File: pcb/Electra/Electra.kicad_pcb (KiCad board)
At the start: 2 copper layers, 100 x 48.5 mm, 79 parts, among them J101 RTC, J102 UART, J201 8-28VIn, J202 USB_B_Micro, J203 Enable VIn, J301 Relay2/D, J401 Relay1/U, J501 S1/U, J502 S2/D, J701 A, J702 A2, J801 RF433, K301 FINDER-36.11, K401 FINDER-36.11, Q301 Q_NPN_EBC, Q401 Q_NPN_EBC, Q801 BSS138, SW601 Flash, SW602 RST, U201 AMS1117-3.3, U202 TPS54202DDCR, U601 ESP-12F

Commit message: PCB Ver 1 completed (TODO: Check)
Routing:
- net +3V3: track 191.2 -> 189.4 mm
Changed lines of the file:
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@@
       (effects (font (size 1 1) (thickness 0.15)))
     )
-    (fp_text value RF433 (at -0.8 -2.4 90) (layer F.SilkS)
+    (fp_text value RF433 (at 0 -4.2 180) (layer F.SilkS)
       (effects (font (size 1 1) (thickness 0.15)))
     )
@@
     (effects (font (size 0.9 0.9) (thickness 0.15)))
   )
-  (gr_text SDL (at 117.4 105.7) (layer F.SilkS)
+  (gr_text SDL (at 122.75 105.7) (layer F.SilkS)
     (effects (font (size 0.9 0.9) (thickness 0.15)))
   )
-  (gr_text SDA (at 117.3 103.2) (layer F.SilkS)
+  (gr_text SDA (at 122.65 102.9) (layer F.SilkS)
     (effects (font (size 0.9 0.9) (thickness 0.15)))
   )
-  (gr_text 3V3 (at 117.4 100.6) (layer F.SilkS)
+  (gr_text 3V3 (at 122.55 100.7) (layer F.SilkS)
     (effects (font (size 0.9 0.9) (thickness 0.15)))
   )
-  (gr_text GND (at 117.3 98) (layer F.SilkS)
+  (gr_text GND (at 119.95 95.85) (layer F.SilkS)
     (effects (font (size 0.9 0.9) (thickness 0.15)))
   )
@@
   (via (at 115.25 116) (size 0.8) (drill 0.4) (layers F.Cu B.Cu) (net 2))
   (via (at 116.25 116) (size 0.8) (drill 0.4) (layers F.Cu B.Cu) (net 2))
-  (via (at 122 106.5) (size 0.8) (drill 0.4) (layers F.Cu B.Cu) (net 2))
-  (via (at 123.25 106.5) (size 0.8) (drill 0.4) (layers F.Cu B.Cu) (net 2))
+  (via (at 122 106.65) (size 0.8) (drill 0.4) (layers F.Cu B.Cu) (net 2))
+  (via (at 123.25 106.7) (size 0.8) (drill 0.4) (layers F.Cu B.Cu) (net 2))
   (via (at 122 107.75) (size 0.8) (drill 0.4) (layers F.Cu B.Cu) (net 2))
   (via (at 123.25 107.75) (size 0.8) (drill 0.4) (layers F.Cu B.Cu) (net 2))
@@
   (segment (start 160 113.12) (end 157.12 113.12) (width 0.5) (layer F.Cu) (net 3))
   (segment (start 157.12 113.12) (end 153.25 109.25) (width 0.5) (layer F.Cu) (net 3))
-  (segment (start 126.6125 92.4745) (end 125.324 91.186) (width 0.7) (layer F.Cu) (net 3))
   (segment (start 128.334 94.25) (end 128.25 94.25) (width 0.7) (layer B.Cu) (net 3))
   (segment (start 126.964 92.964) (end 128.25 94.25) (width 0.7) (layer B.Cu) (net 3))
@@
   (segment (start 153.25 97.75) (end 155.85 95.15) (width 0.5) (layer F.Cu) (net 3))
   (segment (start 155.85 90.091998) (end 155.85 95.15) (width 0.5) (layer F.Cu) (net 3))
-  (segment (start 126.0625 91.9245) (end 125.324 91.186) (width 0.7) (layer F.Cu) (net 3))
-  (segment (start 126.0625 96.1) (end 126.0625 91.9245) (width 0.7) (layer F.Cu) (net 3))
   (segment (start 126.0625 97.8) (end 126.0625 96.1) (width 0.7) (layer F.Cu) (net 3))
   (segment (start 126.4 96.1) (end 128.25 94.25) (width 0.7) (layer F.Cu) (net 3))
   (segment (start 126.0625 96.1) (end 126.4 96.1) (width 0.7) (layer F.Cu) (net 3))
+  (segment (start 125.95 91.812) (end 125.324 91.186) (width 0.7) (layer F.Cu) (net 3))
+  (segment (start 126.0625 96.1) (end 125.95 95.9875) (width 0.7) (layer F.Cu) (net 3))
+  (segment (start 125.95 95.9875) (end 125.95 91.812) (width 0.7) (layer F.Cu) (net 3))
   (via (at 104.8 101.9) (size 0.8) (drill 0.4) (layers F.Cu B.Cu) (net 4))
   (via (at 104.8 104.2) (size 0.8) (drill 0.4) (layers F.Cu B.Cu) (net 4))

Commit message: PCB completed (added silkscreen more)
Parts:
- added G***: LOGO, Custom:Electricity-Causion-6.1mmX6.1mm-logo, B.Cu at (177.0, 100.6)
- added G***: LOGO, Custom:Recycle-electronics-10mmx10mm-logo, B.Cu at (111.5, 99.5)
- added G***: LOGO, Custom:Recycle-electronics-10mmx10mm-logo, F.Cu at (148.0, 98.7)
- added G***: LOGO, Custom:Electricity-Causion-3mmX3mm, F.Cu at (195.0, 102.7)
- J201: value 8-28VIn -> 8-28V
- J202: value USB_B_Micro -> USB
- J301: value Relay2/D -> Relay 2/D
- J401: value Relay1/U -> Relay 1/U
- moved TP301 1.53 mm to (178.3, 109.1)
- moved TP401 1.41 mm to (178.2, 106.5)
- moved C601 0.91 mm to (126.1, 96.0)
- moved C602 0.91 mm to (126.1, 97.7)
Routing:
- net /ESP8266/ADC: track 54.8 -> 56.4 mm
- net +3V3: track 189.4 -> 190.9 mm
- net /Relay1: track 72.9 -> 74.3 mm
- net +5V: track 178.5 -> 179.4 mm
- net /TX: track 43.6 -> 44.5 mm
- net Net-(J601-Pad4): vias 1 -> 0
- net GND: vias 557 -> 556
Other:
- outline, holes or cut-outs redrawn
- board text added: "+"
- board text added: "-"
- board text added: "0603-1210"
- board text added: "10K"
- board text added: "10x10"
- board text added: "CAUTION! AC Voltage"
- board text added: "If you are reading this, I hope you have a nice day!"
- board text added: "NC"
- board text added: "NO"
- board text added: "R20X"
- board text removed: "CAUTION! AC Main"

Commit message: Pcb completed with 3D model
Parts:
- removed the G*** at (111.5, 99.5)
- removed the G*** at (148.0, 98.7)
- moved J201 2.22 mm to (108.0, 81.0)
- moved J801 1.40 mm to (146.6, 86.7)
- moved C208 0.69 mm to (123.2, 83.3)
- moved C203 0.56 mm to (116.8, 83.3)
- moved J501 0.44 mm to (154.5, 76.3)
- moved J701 0.44 mm to (136.7, 76.3)
- moved J702 0.44 mm to (128.1, 76.3)
- moved J502 0.44 mm to (145.6, 76.3)
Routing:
- net /Switch1: track 66.1 -> 49.5 mm, vias 0 -> 1
- net +3V3: track 190.9 -> 196.3 mm
- net /Switch2: track 43.9 -> 39.3 mm, vias 0 -> 1
- net +5V: track 179.4 -> 176.2 mm
- net Net-(J702-Pad1): track 8.60 -> 10.9 mm, vias 0 -> 2
- net /ESP8266/ADC: track 56.4 -> 55.3 mm
- net /ESP8266/GPIO0: track 49.2 -> 48.6 mm
- net GND: vias 556 -> 569
- net +VDC: vias 11 -> 18

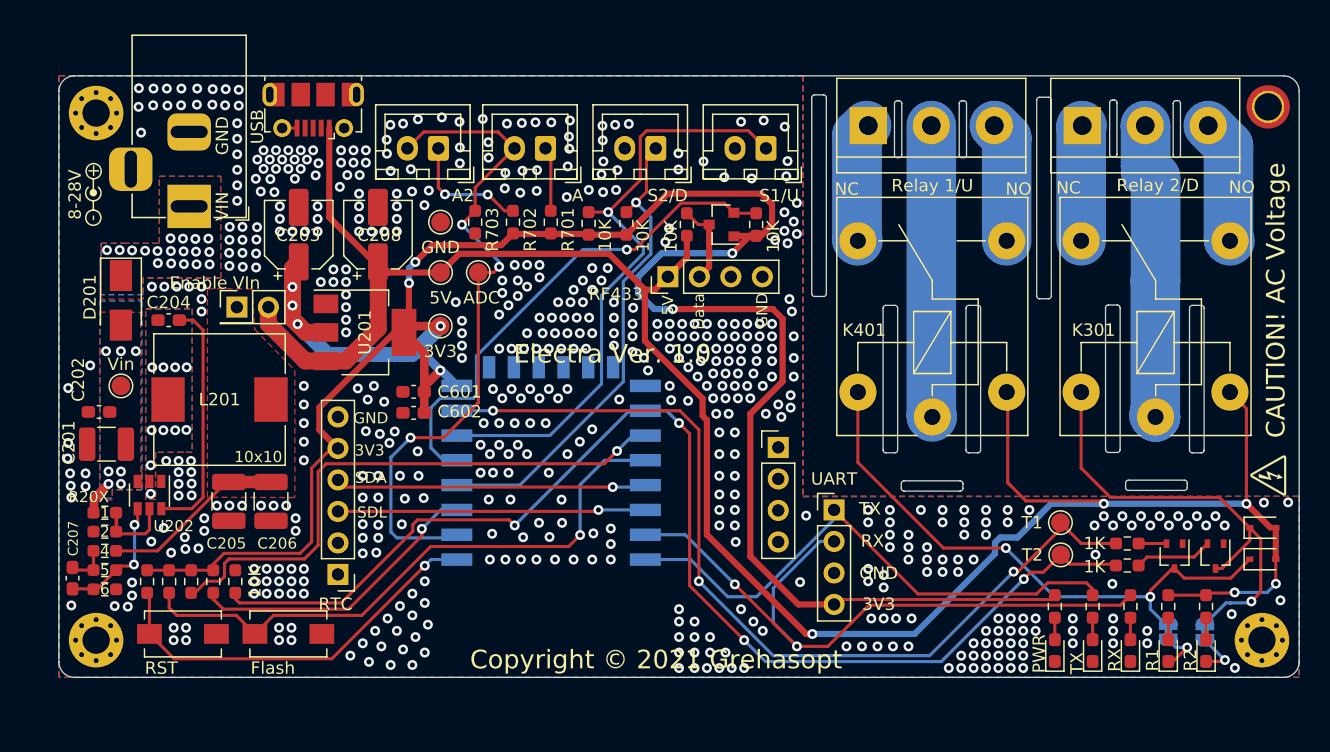
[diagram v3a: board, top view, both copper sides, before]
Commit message: Panel added, gerbs added
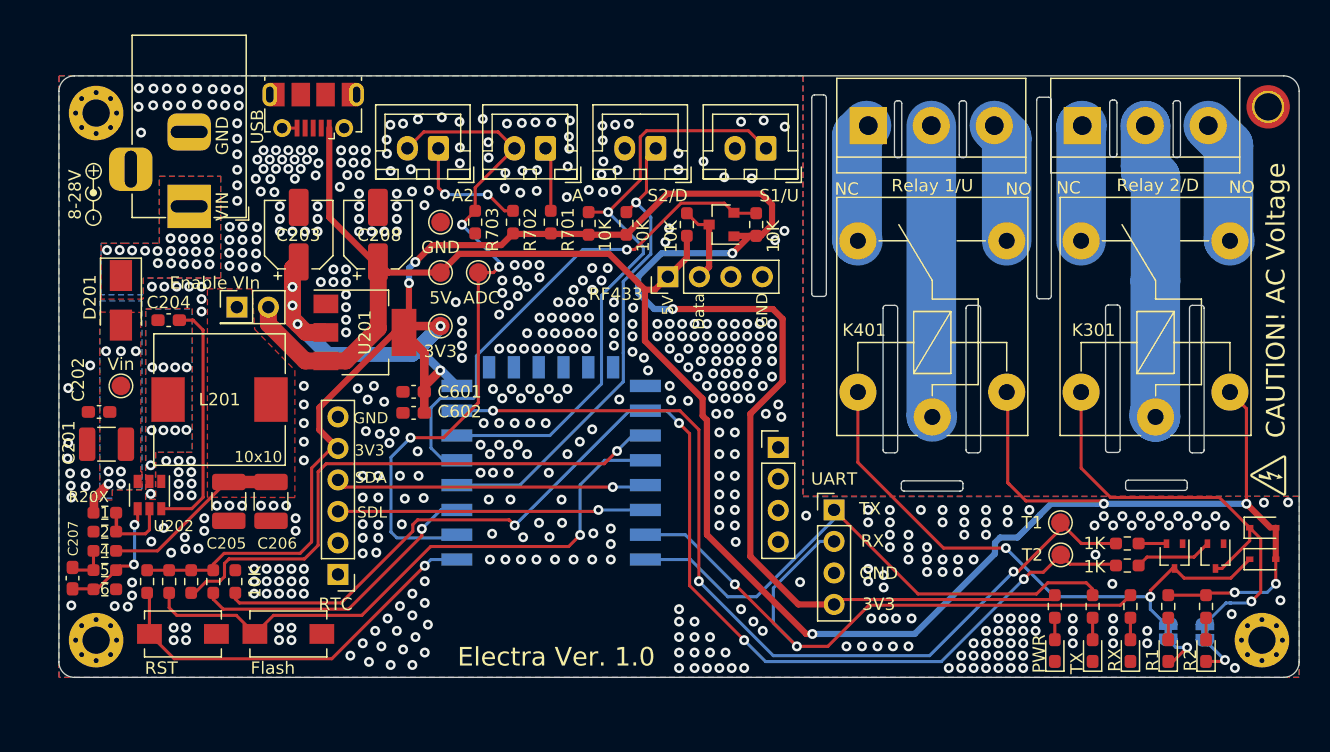
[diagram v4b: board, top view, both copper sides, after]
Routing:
- net GND: vias 569 -> 555
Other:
- board text removed: "Copyright © 2021 Grehasopt"
- board text removed: "JLCJLCJLCJLC"
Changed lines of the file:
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@@
   (general
     (thickness 1.6)
-    (drawings 145)
-    (tracks 1093)
+    (drawings 143)
+    (tracks 1079)
     (zones 0)
     (modules 81)
@@
     (pad_to_mask_clearance 0)
     (aux_axis_origin 0 0)
+    (grid_origin 97.5 70.5)
     (visible_elements FFFFEF7F)
     (pcbplotparams
       (layerselection 0x010f0_ffffffff)
       (usegerberextensions false)
-      (usegerberattributes true)
-      (usegerberadvancedattributes true)
-      (creategerberjobfile true)
+      (usegerberattributes false)
+      (usegerberadvancedattributes false)
+      (creategerberjobfile false)
       (excludeedgelayer true)
       (linewidth 0.100000)
@@
       (drillshape 0)
       (scaleselection 1)
-      (outputdirectory "gerbers/"))
+      (outputdirectory "gerber/single/"))
   )
   (net 0 "")
@@
       (effects (font (size 0.8 0.8) (thickness 0.12)))
     )
-    (pad 2 smd roundrect (at 1.5625 0 180) (size 1.325 2.7) (layers F.Cu F.Paste F.Mask) (roundrect_rratio 0.1886784905660377)
+    (pad 2 smd roundrect (at 1.5625 0 180) (size 1.325 2.7) (layers F.Cu F.Paste F.Mask) (roundrect_rratio 0.1886769811320755)
       (net 2 GND))
-    (pad 1 smd roundrect (at -1.5625 0 180) (size 1.325 2.7) (layers F.Cu F.Paste F.Mask) (roundrect_rratio 0.1886784905660377)
+    (pad 1 smd roundrect (at -1.5625 0 180) (size 1.325 2.7) (layers F.Cu F.Paste F.Mask) (roundrect_rratio 0.1886769811320755)
       (net 1 "Net-(C201-Pad1)"))
     (model ${KISYS3DMOD}/Capacitor_SMD.3dshapes/C_1210_3225Metric.wrl
@@
       (effects (font (size 0.8 0.8) (thickness 0.12)))
     )
-    (pad 1 smd roundrect (at -1.5625 0 90) (size 1.325 2.7) (layers F.Cu F.Paste F.Mask) (roundrect_rratio 0.1886784905660377)
+    (pad 1 smd roundrect (at -1.5625 0 90) (size 1.325 2.7) (layers F.Cu F.Paste F.Mask) (roundrect_rratio 0.1886769811320755)
       (net 2 GND))
-    (pad 2 smd roundrect (at 1.5625 0 90) (size 1.325 2.7) (layers F.Cu F.Paste F.Mask) (roundrect_rratio 0.1886784905660377)
+    (pad 2 smd roundrect (at 1.5625 0 90) (size 1.325 2.7) (layers F.Cu F.Paste F.Mask) (roundrect_rratio 0.1886769811320755)
       (net 6 "Net-(C205-Pad2)"))
     (model ${KISYS3DMOD}/Capacitor_SMD.3dshapes/C_1210_3225Metric.wrl
@@
       (effects (font (size 0.8 0.8) (thickness 0.12)))
     )
-    (pad 2 smd roundrect (at 1.5625 0 90) (size 1.325 2.7) (layers F.Cu F.Paste F.Mask) (roundrect_rratio 0.1886784905660377)
+    (pad 2 smd roundrect (at 1.5625 0 90) (size 1.325 2.7) (layers F.Cu F.Paste F.Mask) (roundrect_rratio 0.1886769811320755)
       (net 6 "Net-(C205-Pad2)"))
-    (pad 1 smd roundrect (at -1.5625 0 90) (size 1.325 2.7) (layers F.Cu F.Paste F.Mask) (roundrect_rratio 0.1886784905660377)
+    (pad 1 smd roundrect (at -1.5625 0 90) (size 1.325 2.7) (layers F.Cu F.Paste F.Mask) (roundrect_rratio 0.1886769811320755)
       (net 2 GND))
     (model ${KISYS3DMOD}/Capacitor_SMD.3dshapes/C_1210_3225Metric.wrl
@@
     (effects (font (size 1 1) (thickness 0.25)))
   )
-  (gr_text JLCJLCJLCJLC (at 196.3 90.25 90) (layer B.SilkS)
-    (effects (font (size 1 1) (thickness 0.25)) (justify mirror))
-  )
   (gr_text "CAUTION! AC Voltage" (at 195.625 88.6 90) (layer F.SilkS)
     (effects (font (size 1.5 1.5) (thickness 0.3)))
@@
     (effects (font (size 1 1) (thickness 0.15)))
   )
-  (gr_text "Copyright © 2021 Grehasopt " (at 145.65 117.575) (layer F.SilkS)
-    (effects (font (size 1.5 1.5) (thickness 0.3)))
-  )
-  (gr_text "Electra Ver. 1.0" (at 142.125 92.925) (layer F.SilkS)
+  (gr_text "Electra Ver. 1.0" (at 137.6 117.35) (layer F.SilkS)
     (effects (font (size 1.5 1.5) (thickness 0.3)))
   )
@@
   (via (at 154.5 97.75) (size 0.8) (drill 0.4) (layers F.Cu B.Cu) (net 2))
   (via (at 155.5 97) (size 0.8) (drill 0.4) (layers F.Cu B.Cu) (net 2))
-  (via (at 156.5 96.25) (size 0.8) (drill 0.4) (layers F.Cu B.Cu) (net 2))
   (via (at 155.75 98) (size 0.8) (drill 0.4) (layers F.Cu B.Cu) (net 2))
-  (via (at 156.5 97.25) (size 0.8) (drill 0.4) (layers F.Cu B.Cu) (net 2))
   (via (at 155.25 83.75) (size 0.8) (drill 0.4) (layers F.Cu B.Cu) (net 2))
-  (via (at 156 83) (size 0.8) (drill 0.4) (layers F.Cu B.Cu) (net 2))
-  (via (at 156.75 82.25) (size 0.8) (drill 0.4) (layers F.Cu B.Cu) (net 2))
-  (via (at 156.25 84) (size 0.8) (drill 0.4) (layers F.Cu B.Cu) (net 2))
-  (via (at 157 83.25) (size 0.8) (drill 0.4) (layers F.Cu B.Cu) (net 2))
-  (via (at 156 81.5) (size 0.8) (drill 0.4) (layers F.Cu B.Cu) (net 2))
-  (via (at 157 80.75) (size 0.8) (drill 0.4) (layers F.Cu B.Cu) (net 2))
-  (via (at 156.75 94.75) (size 0.8) (drill 0.4) (layers F.Cu B.Cu) (net 2))
-  (via (at 156.75 93.25) (size 0.8) (drill 0.4) (layers F.Cu B.Cu) (net 2))
-  (via (at 156.75 91.5) (size 0.8) (drill 0.4) (layers F.Cu B.Cu) (net 2))
   (via (at 112 71.625) (size 0.8) (drill 0.4) (layers F.Cu B.Cu) (net 2))
   (via (at 110.95 71.575) (size 0.8) (drill 0.4) (layers F.Cu B.Cu) (net 2))
@@
   (via (at 111.875 80.575) (size 0.8) (drill 0.4) (layers F.Cu B.Cu) (net 2))
   (via (at 104.125 75.075) (size 0.8) (drill 0.4) (layers F.Cu B.Cu) (net 2))
-  (via (at 156.4 88.5) (size 0.8) (drill 0.4) (layers F.Cu B.Cu) (net 2))
-  (via (at 156.6 89.5) (size 0.8) (drill 0.4) (layers F.Cu B.Cu) (net 2))
   (via (at 143.8 89.2) (size 0.8) (drill 0.4) (layers F.Cu B.Cu) (net 2))
   (via (at 146.4 83.9) (size 0.8) (drill 0.4) (layers F.Cu B.Cu) (net 2))
@@
   (via (at 151.15 78.675) (size 0.8) (drill 0.4) (layers F.Cu B.Cu) (net 2))
   (via (at 153.35 78.775) (size 0.8) (drill 0.4) (layers F.Cu B.Cu) (net 2))
-  (via (at 156.15 78.6) (size 0.8) (drill 0.4) (layers F.Cu B.Cu) (net 2))
-  (via (at 156.25 77.375) (size 0.8) (drill 0.4) (layers F.Cu B.Cu) (net 2))
-  (via (at 156.025 74.6) (size 0.8) (drill 0.4) (layers F.Cu B.Cu) (net 2))
   (via (at 154.325 74.1) (size 0.8) (drill 0.4) (layers F.Cu B.Cu) (net 2))
   (via (at 152.5 74.2) (size 0.8) (drill 0.4) (layers F.Cu B.Cu) (net 2))
@@
   (via (at 112.3 82.675) (size 0.8) (drill 0.4) (layers F.Cu B.Cu) (net 2))
   (via (at 113.475 82.7) (size 0.8) (drill 0.4) (layers F.Cu B.Cu) (net 2))
+  (via (at 156.025 74.6) (size 0.8) (drill 0.4) (layers F.Cu B.Cu) (net 2))
+  (via (at 156 83) (size 0.8) (drill 0.4) (layers F.Cu B.Cu) (net 2))
   (segment (start 117.413998 91.186) (end 119.024 91.186) (width 1.37) (layer F.Cu) (net 3))
   (via (at 125.73 87.21) (size 0.8) (drill 0.4) (layers F.Cu B.Cu) (net 3))

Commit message: Rev 2 completed, todo check all and remove not needed filed
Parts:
- removed C206: 22uF, Capacitor_SMD:C_1210_3225Metric_Pad1.33x2.70mm_HandSolder
- removed C207: 75pF, Capacitor_SMD:C_0603_1608Metric_Pad1.08x0.95mm_HandSolder
- removed C208: 100uF, Capacitor_SMD:CP_Elec_5x5.4
- removed C601: 0.1uF, Capacitor_SMD:C_0603_1608Metric_Pad1.08x0.95mm_HandSolder
- removed C602: 47uF, Capacitor_SMD:C_0603_1608Metric_Pad1.08x0.95mm_HandSolder
- removed D401: R1, LED_SMD:LED_0603_1608Metric_Pad1.05x0.95mm_HandSolder
- removed D402: 200mA, Diode_SMD:D_SOD-323
- removed D601: TX, LED_SMD:LED_0603_1608Metric_Pad1.05x0.95mm_HandSolder
- removed D602: RX, LED_SMD:LED_0603_1608Metric_Pad1.05x0.95mm_HandSolder
- removed the G*** at (177.0, 100.6)
- removed the G*** at (195.0, 102.7)
- removed J203: Enable VIn, Connector_PinHeader_2.54mm:PinHeader_2x01_P2.54mm_Vertical
- removed J501: S1/U, Connector_JST:JST_XH_B2B-XH-A_1x02_P2.50mm_Vertical
- removed J502: S2/D, Connector_JST:JST_XH_B2B-XH-A_1x02_P2.50mm_Vertical
- removed J702: A2, Connector_JST:JST_XH_B2B-XH-A_1x02_P2.50mm_Vertical
- removed JP401: Jumper_NC_Small, Jumper:SolderJumper-2_P1.3mm_Bridged_RoundedPad1.0x1.5mm
- removed K401: FINDER-36.11, Relay_THT:Relay_SPDT_Finder_36.11
- removed L201: 15uH, Inductor_SMD:L_10.4x10.4_H4.8
- removed Q401: Q_NPN_EBC, Package_TO_SOT_SMD:SOT-323_SC-70
- removed R202: 105K, Resistor_SMD:R_0603_1608Metric_Pad0.98x0.95mm_HandSolder
- removed R203, R604, R607: 80, Resistor_SMD:R_0603_1608Metric_Pad0.98x0.95mm_HandSolder
- removed R204: 49.9, Resistor_SMD:R_0603_1608Metric_Pad0.98x0.95mm_HandSolder
- removed R205: 100K, Resistor_SMD:R_0603_1608Metric_Pad0.98x0.95mm_HandSolder
- removed R206: 13.3K, Resistor_SMD:R_0603_1608Metric_Pad0.98x0.95mm_HandSolder
- removed R605, R606: 10K, Resistor_SMD:R_0603_1608Metric_Pad0.98x0.95mm_HandSolder
- removed R703: 1K, Resistor_SMD:R_0603_1608Metric_Pad0.98x0.95mm_HandSolder
- removed SW601: Flash, Button_Switch_SMD:SW_SPST_EVQPE1
- removed SW602: RST, Button_Switch_SMD:SW_SPST_EVQPE1
- removed TP401: T1, TestPoint:TestPoint_Pad_D1.5mm
- removed TP701: ADC, TestPoint:TestPoint_Pad_D1.5mm
- removed U601: ESP-12F, RF_Module:ESP-12E
- added C501: 0.1uF, Capacitor_SMD:C_0603_1608Metric_Pad1.08x0.95mm_HandSolder, F.Cu at (130.9, 90.5)
- added C502: 47uF, Capacitor_SMD:C_1206_3216Metric_Pad1.33x1.80mm_HandSolder, F.Cu at (130.0, 92.4)
- added D203: 1A, Diode_SMD:D_SMA_Handsoldering, F.Cu at (110.5, 97.4)
- added D204: PWR, LED_SMD:LED_0603_1608Metric_Pad1.05x0.95mm_HandSolder, F.Cu at (177.1, 117.2)
- added D501: TX, LED_SMD:LED_0603_1608Metric_Pad1.05x0.95mm_HandSolder, F.Cu at (183.4, 117.2)
- added D502: RX, LED_SMD:LED_0603_1608Metric_Pad1.05x0.95mm_HandSolder, F.Cu at (180.3, 117.2)
- added D801: R1, LED_SMD:LED_0603_1608Metric_Pad1.05x0.95mm_HandSolder, F.Cu at (189.4, 117.2)
- added D802: 200mA, Diode_SMD:D_MiniMELF, F.Cu at (186.1, 106.1)
- added G***: LOGO, Custom:dc-barrel-positive-polarity-bold-5.1x5, F.Cu at (99.4, 78.8)
- added G***: LOGO, Custom:Electricity-Causion-6.1mmX6.1mm-logo, B.Cu at (176.9, 92.1)
- added G***: LOGO, Custom:Electricity-Causion-6.1mmX6.1mm-logo, F.Cu at (194.0, 103.5)
- added J103: Extra2, Connector_PinHeader_2.54mm:PinHeader_1x03_P2.54mm_Vertical, F.Cu at (100.0, 104.3)
- added J104: UART, Connector_PinHeader_2.54mm:PinHeader_1x04_P2.54mm_Vertical, F.Cu at (160.1, 106.1)
- added J402: S2/D, Connector_JST:JST_XH_B2B-XH-A_1x02_P2.50mm_Vertical, F.Cu at (146.3, 76.4)
- added J601: A, Connector_JST:JST_XH_B2B-XH-A_1x02_P2.50mm_Vertical, F.Cu at (137.8, 76.4)
- added J602: A2, Connector_JST:JST_XH_B2B-XH-A_1x02_P2.50mm_Vertical, F.Cu at (129.4, 76.4)
- added JP201: USB-In, Jumper:SolderJumper-2_P1.3mm_Bridged_RoundedPad1.0x1.5mm, B.Cu at (119.1, 78.6)
- added JP801: R1, Jumper:SolderJumper-2_P1.3mm_Bridged_RoundedPad1.0x1.5mm, B.Cu at (186.3, 109.7)
- added K801: FINDER-36.11, Relay_THT:Relay_SPDT_Finder_36.11, F.Cu at (185.9, 98.9)
- added R503: 10K, Resistor_SMD:R_0603_1608Metric_Pad0.98x0.95mm_HandSolder, F.Cu at (146.0, 82.4)
- added R504: 15, Resistor_SMD:R_0805_2012Metric_Pad1.20x1.40mm_HandSolder, F.Cu at (183.4, 113.7)
- added R505: 10K, Resistor_SMD:R_0603_1608Metric_Pad0.98x0.95mm_HandSolder, F.Cu at (150.6, 82.4)
- added R506: 10K, Resistor_SMD:R_0603_1608Metric_Pad0.98x0.95mm_HandSolder, F.Cu at (152.1, 82.4)
- added R507: 15, Resistor_SMD:R_0805_2012Metric_Pad1.20x1.40mm_HandSolder, F.Cu at (180.3, 113.7)
- added SW501: Flash, Button_Switch_SMD:SW_SPST_CK_RS282G05A3, F.Cu at (169.4, 116.9)
- added SW502: RST, Button_Switch_SMD:SW_SPST_CK_RS282G05A3, F.Cu at (169.4, 112.6)
- added TP601: ADC, TestPoint:TestPoint_Pad_D1.5mm, F.Cu at (127.8, 85.6)
- added TP801: T1, TestPoint:TestPoint_Pad_D1.5mm, F.Cu at (133.1, 85.6)
- added U501: ESP-12F, RF_Module:ESP-12E, B.Cu at (139.4, 106.8)
- C201: value 10uF -> 100uF; footprint Capacitor_SMD:C_1210_3225Metric_Pad1.33x2.70mm_HandSolder -> Capacitor_SMD:CP_Elec_6.3x5.4
- C202: value 0.1uF -> 10uF; footprint Capacitor_SMD:C_0603_1608Metric_Pad1.08x0.95mm_HandSolder -> Capacitor_SMD:C_0805_2012Metric_Pad1.18x1.45mm_HandSolder
- C203: value 100uF -> 10uF; footprint Capacitor_SMD:CP_Elec_5x5.4 -> Capacitor_SMD:C_0805_2012Metric_Pad1.18x1.45mm_HandSolder
- C204: value 0.1uF -> 100uF; footprint Capacitor_SMD:C_0603_1608Metric_Pad1.08x0.95mm_HandSolder -> Capacitor_SMD:CP_Elec_6.3x5.4
- C205: value 22uF -> 100uF; footprint Capacitor_SMD:C_1210_3225Metric_Pad1.33x2.70mm_HandSolder -> Capacitor_SMD:CP_Elec_6.3x5.4
- D201: value DIODE -> 1A; footprint Diode_SMD:D_SMA -> Diode_SMD:D_SMA_Handsoldering
- D202: value PWR -> 1A; footprint LED_SMD:LED_0603_1608Metric_Pad1.05x0.95mm_HandSolder -> Diode_SMD:D_SMA_Handsoldering
- D302: footprint Diode_SMD:D_SOD-323 -> Diode_SMD:D_MiniMELF
- J101: value RTC -> Extra1; footprint Connector_PinHeader_2.54mm:PinHeader_1x06_P2.54mm_Vertical -> Connector_PinHeader_2.54mm:PinHeader_1x03_P2.54mm_Vertical
- J102: value UART -> RTC; footprint Connector_PinHeader_2.54mm:PinHeader_1x04_P2.54mm_Vertical -> Connector_PinHeader_2.54mm:PinHeader_1x06_P2.54mm_Vertical
- J201: value 8-28V -> USB; footprint Connector_BarrelJack:BarrelJack_Horizontal -> Connector_USB:USB_Micro-B_Molex-105017-0001
- J202: value USB -> 7-12V; footprint Connector_USB:USB_Micro-B_Molex-105017-0001 -> Connector_BarrelJack:BarrelJack_Horizontal
- J401: value Relay 1/U -> S1/U; footprint TerminalBlock:TerminalBlock_bornier-3_P5.08mm -> Connector_JST:JST_XH_B2B-XH-A_1x02_P2.50mm_Vertical
- J701: value A -> RF433; footprint Connector_JST:JST_XH_B2B-XH-A_1x02_P2.50mm_Vertical -> Connector_PinHeader_2.54mm:PinHeader_1x04_P2.54mm_Vertical
- J801: value RF433 -> Relay 1/U; footprint Connector_PinHeader_2.54mm:PinHeader_1x04_P2.54mm_Vertical -> TerminalBlock:TerminalBlock_bornier-3_P5.08mm
- JP301: value Jumper_NC_Small -> R2
- Q801: value BSS138 -> Q_NPN_EBC; footprint Package_TO_SOT_SMD:SOT-23 -> Package_TO_SOT_SMD:SOT-323_SC-70
- R201: value 511K -> 82
- R302: value 150 -> 68
- R401: value 1K -> 10K
- R402: value 150 -> 10K
- R601: value 10K -> 3.3K
- R602: value 10K -> 7.5K
- R603, R801: value 10K -> 1K
- R701: value 3.57K -> 1K
- R702: value 7.5K -> 2K
- R802: value 10K -> 68
- TP203: value 3V3 -> 5V
- TP204: value 5V -> 3V3
- U201: value AMS1117-3.3 -> AMS1117-5.0
- U202: value TPS54202DDCR -> AMS1117-3.3; footprint Package_TO_SOT_SMD:SOT-23-6 -> Package_TO_SOT_SMD:SOT-223-3_TabPin2
- moved D202 78.8 mm to (104.8, 87.1), turned to 270 degrees
- moved R201 76.2 mm to (177.0, 113.9), turned to 90 degrees
- moved R402 53.7 mm to (143.0, 82.4), turned to 90 degrees
- moved TP301 53.3 mm to (130.4, 85.6)
- moved R802 51.9 mm to (189.4, 113.9), turned to 270 degrees
- moved Q801 48.8 mm to (192.7, 107.8), turned to 0 degrees
- moved R401 46.9 mm to (144.5, 82.4), turned to 90 degrees
- moved R602 45.4 mm to (139.7, 82.4), turned to 270 degrees
- moved R601 45.2 mm to (141.2, 82.4), turned to 270 degrees
- moved R801 41.6 mm to (186.2, 108.5), turned to 180 degrees
- moved J102 41.0 mm to (119.4, 110.9), turned to 180 degrees
- moved R603 40.3 mm to (138.1, 82.4)
- moved J801 35.4 mm to (180.3, 75.7), turned to 0 degrees
- moved D302 26.4 mm to (168.2, 106.1)
- moved C205 24.8 mm to (120.1, 81.7), turned to 0 degrees
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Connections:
- C202 pad 1: Net-(C201-Pad1) -> +3V3
- C203 pad 1: +3V3 -> +5V
- C204 pad 1: Net-(C204-Pad1) -> +3V3
- C204 pad 2: Net-(C204-Pad2) -> GND
- C205 pad 1: GND -> +5V
- C205 pad 2: Net-(C205-Pad2) -> GND
- D202 pad 1: GND -> +VDC
- D202 pad 2: Net-(D202-Pad2) -> Net-(C201-Pad1)
- J101 pad 1: Net-(J101-Pad1) -> +3V3
- J101 pad 2: Net-(J101-Pad2) -> /Extra1
- J101 pad 3: /L-SDL -> GND
- J102 pad 1: /TX -> Net-(J102-Pad1)
- J102 pad 2: /RX -> Net-(J102-Pad2)
- J102 pad 3: GND -> /L-SDL
- J102 pad 4: +3V3 -> /L-SDA
- J201 pad 1: +VDC -> Net-(J201-Pad1)
- J201 pad 2: GND -> Net-(J201-Pad2)
- J201 pad 3: (no net) -> Net-(J201-Pad3)
- J202 pad 1: +5V -> +VDC
- J202 pad 2: Net-(J202-Pad2) -> GND
- J202 pad 3: Net-(J202-Pad3) -> (no net)
- J401 pad 1: /Relay1/Relay-Normal-Close -> /Switch1
- J401 pad 2: /Relay1/Relay-Common -> GND
- J701 pad 1: Net-(J701-Pad1) -> +5V
- J701 pad 2: /ESP8266/ADC -> Net-(J701-Pad2)
- J801 pad 1: +5V -> /Relay1/Relay-Normal-Close
- J801 pad 2: Net-(J801-Pad2) -> /Relay1/Relay-Common
- J801 pad 3: Net-(J801-Pad3) -> /Relay1/Relay-Normal-Open
- Q801 pad 1: +3V3 -> GND
- Q801 pad 2: /ESP8266/GPIO14 -> Net-(Q801-Pad2)
- Q801 pad 3: Net-(J801-Pad2) -> Net-(D802-Pad1)
- R201 pad 1: Net-(C201-Pad1) -> Net-(D204-Pad2)
- R201 pad 2: Net-(R201-Pad2) -> +3V3
- R401 pad 1: Net-(Q401-Pad2) -> +3V3
- R401 pad 2: /Relay1 -> /Switch1
- R402 pad 1: +5V -> +3V3
- R402 pad 2: Net-(D401-Pad2) -> /Switch2
- R501 pad 1: +3V3 -> /ESP8266/GPIO0
- R501 pad 2: /Switch1 -> +3V3
- R502 pad 1: +3V3 -> /ESP8266/~RST
- R502 pad 2: /Switch2 -> +3V3
- R601 pad 1: /ESP8266/GPIO0 -> Net-(J601-Pad1)
- R602 pad 1: /ESP8266/~RST -> Net-(J602-Pad1)
- R603 pad 1: +3V3 -> /ESP8266/ADC
- R603 pad 2: Net-(R603-Pad2) -> GND
- R701 pad 1: Net-(J701-Pad1) -> Net-(J701-Pad2)
- R701 pad 2: +3V3 -> /ESP8266/GPIO14
- R702 pad 1: Net-(J702-Pad1) -> /ESP8266/GPIO14
- R702 pad 2: +3V3 -> GND
- R801 pad 1: +3V3 -> Net-(Q801-Pad2)
- R801 pad 2: /ESP8266/GPIO14 -> /Relay1
- R802 pad 2: Net-(J801-Pad2) -> Net-(D801-Pad2)
- TP203 pad 1: +3V3 -> +5V
- TP204 pad 1: +5V -> +3V3
- U201 pad 2: +3V3 -> +5V
- U201 pad 3: +5V -> Net-(C201-Pad1)
- U202 pad 2: Net-(C204-Pad1) -> +3V3
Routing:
- net /Extra2: track 0.00 -> 83.0 mm, vias 0 -> 3
- net /Extra1: track 0.00 -> 70.8 mm, vias 0 -> 2
- net Net-(D402-Pad1): track 46.9 -> 0.00 mm, vias 2 -> 0
- net /ESP8266/GPIO2: track 46.0 -> 0.00 mm, vias 1 -> 0
- net Net-(R503-Pad2): track 0.00 -> 42.8 mm, vias 0 -> 3
- net /ESP8266/~RST: track 32.3 -> 74.3 mm, vias 1 -> 2
- net /Relay2: track 98.6 -> 67.3 mm, vias 4 -> 5
- net Net-(D802-Pad1): track 0.00 -> 27.1 mm, vias 0 -> 1
- net Net-(R603-Pad2): track 24.1 -> 0.00 mm, vias 1 -> 0
- net Net-(D301-Pad1): track 4.22 -> 24.5 mm
- net Net-(C204-Pad2): track 19.7 -> 0.00 mm
- net +3V3: track 196.3 -> 177.4 mm, vias 9 -> 2
- net Net-(C205-Pad2): track 15.4 -> 0.00 mm
- net Net-(J602-Pad1): track 0.00 -> 15.4 mm
- net Net-(J701-Pad2): track 0.00 -> 12.6 mm, vias 0 -> 1
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- removed copper zone on B.Cu, net Net-(C201-Pad1)
- removed copper zone on B.Cu, net Net-(C204-Pad1)
- removed copper zone on F.Cu, net Net-(C204-Pad1)
- removed copper zone on F.Cu, net Net-(C205-Pad2)
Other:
- outline, holes or cut-outs redrawn
- board text added: "10"
- board text added: "2"
- board text added: "A"
- board text added: "A2"
- board text added: "AC Main Voltage"
- board text added: "ADC"
- board text added: "CAUTION!"
- board text added: "CAUTION! AC Main Voltage"
- board text added: "Electra Rev. 2.0"
- board text added: "Extra1"
- board text added: "Extra2"
- board text added: "Flash"
- board text added: "PWR"
- board text added: "R1"
- board text added: "R2"
- board text added: "RF433"
- board text added: "RST"
- board text added: "RTC"
- board text added: "Relay 1/U"
- board text added: "Relay 2/D"
- board text added: "S1/U"
- board text added: "S2/D"
- board text added: "T1"
- board text added: "T2"
- board text added: "UART"
- board text added: "USB"
- board text added: "USB-In"
- board text removed: "-"
- board text removed: "0603-1210"
- board text removed: "10K"
- board text removed: "10x10"
- board text removed: "CAUTION! AC Voltage"
- board text removed: "Electra Ver. 1.0"
- board text removed: "R20X"
- board text removed: "VIN"

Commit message: IMPORTANT! REV 2 completed! Send to fabrication
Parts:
- added G***: LOGO, Custom:Recycle-electronics-10mmx10mm-logo, B.Cu at (109.2, 94.5)
- JP201: value USB-In -> USB-IN
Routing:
- net Net-(J701-Pad2): track 12.6 -> 17.3 mm
- net /Switch1: track 54.4 -> 57.4 mm
- net +3V3: track 177.4 -> 178.8 mm, vias 2 -> 4
- net GND: vias 391 -> 367
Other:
- board text added: "Copyright © 2021 Grehasopt"
- board text removed: "USB-In"
